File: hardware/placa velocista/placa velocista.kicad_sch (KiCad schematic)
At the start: 22 parts, among them J1 Conn_01x07, J5 Screw_Terminal_01x02, SW2 SW_SPDT, SW3 s, U1 ESP32_CDN, U2 LM7805

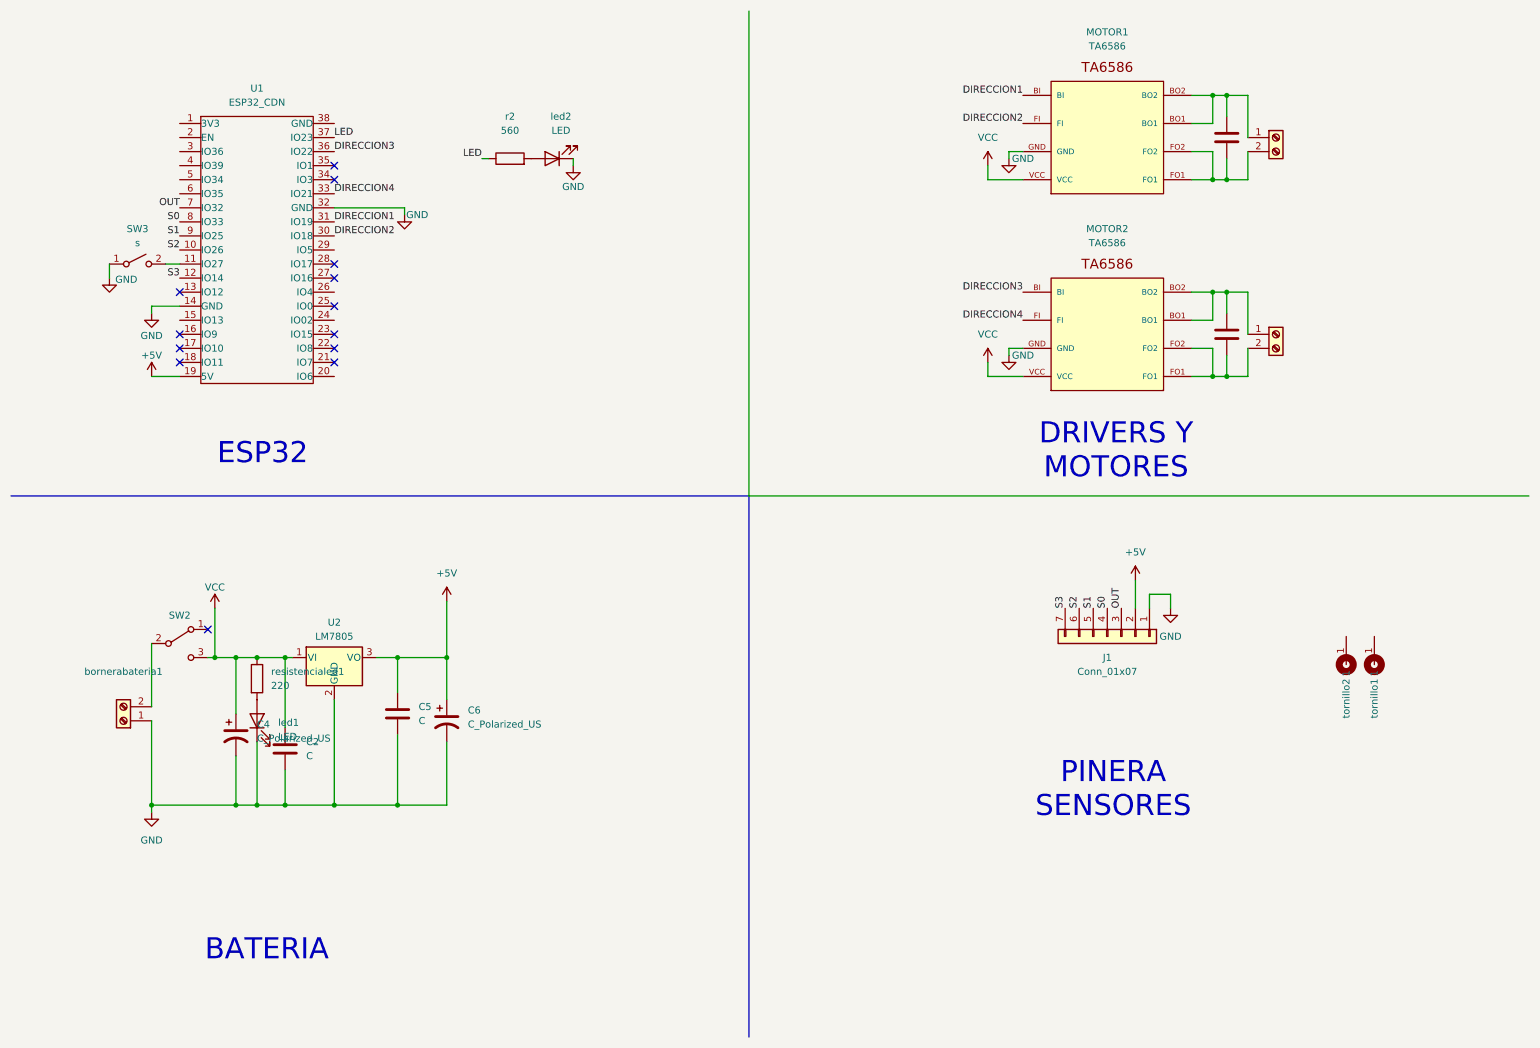
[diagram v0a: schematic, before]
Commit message: Agregue divisor de tension
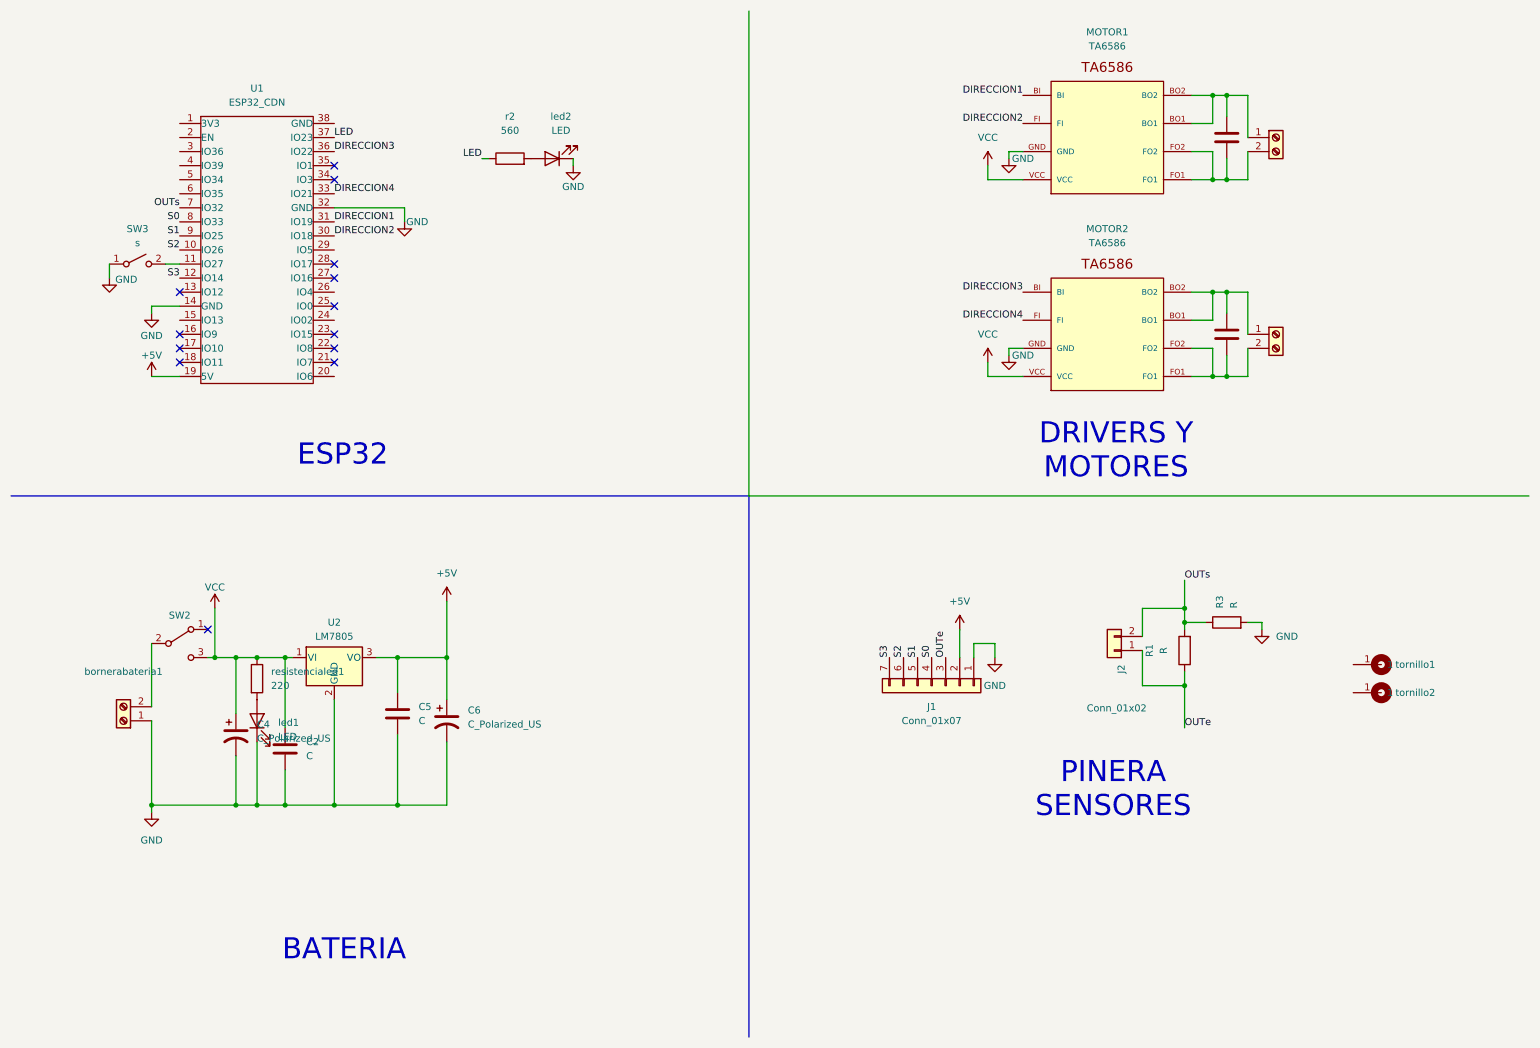
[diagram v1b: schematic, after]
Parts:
- added J2: Conn_01x02, Connector_PinHeader_2.54mm:PinHeader_1x02_P2.54mm_Vertical, symbol Connector_Generic:Conn_01x02
- added R1, R3: R, EESTN5:R_0805, symbol Device:R
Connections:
- net GND: now also R3.2
- net OUT renamed OUTe
- net OUTe: now also J2.1 (Pin_1), R1.1; no longer U1.7 (IO32)
- new net OUTs: J2.2 (Pin_2), R1.2, R3.1, U1.7 (IO32)
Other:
- moved on the sheet: J1, tornillo1, tornillo2
